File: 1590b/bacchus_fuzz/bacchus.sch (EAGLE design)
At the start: 27 parts, among them J1 DC_MONO, Q1 NPN, Q2 NPN

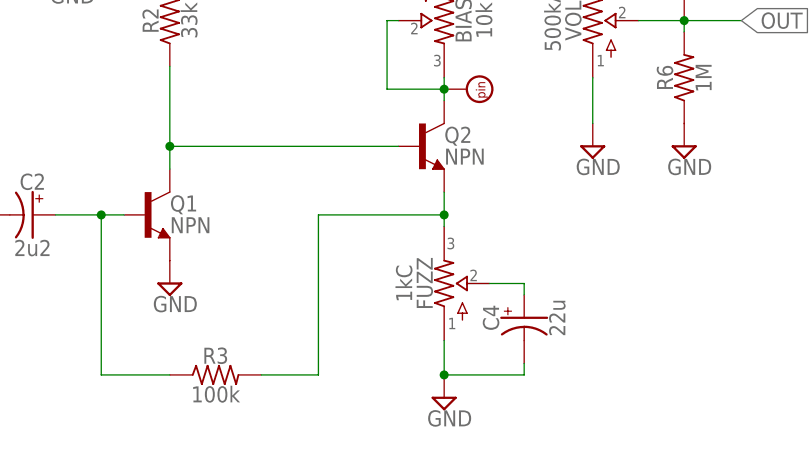
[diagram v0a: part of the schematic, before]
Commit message: added SQUONK (envelope filter)
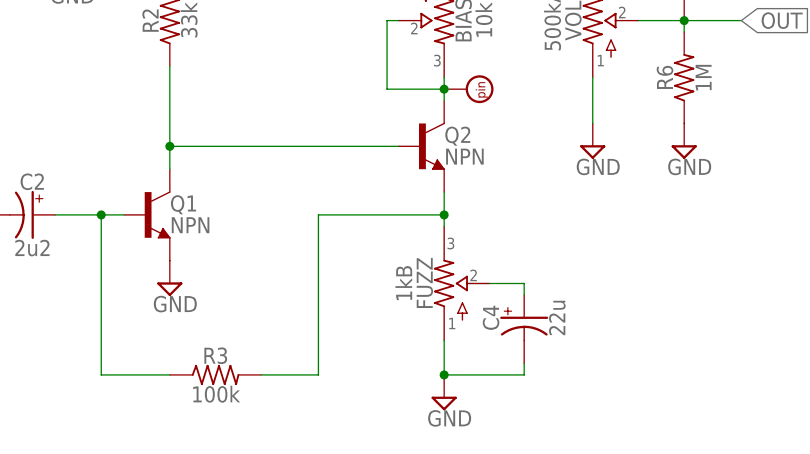
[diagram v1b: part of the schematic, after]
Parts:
- FUZZ: value 1kC -> 1kB
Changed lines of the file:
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@@
 <setting verticaltext="up"/>
 </settings>
-<grid distance="0.05" unitdist="inch" unit="inch" style="lines" multiple="1" display="no" altdistance="0.01" altunitdist="inch" altunit="inch"/>
+<grid distance="0.1" unitdist="inch" unit="inch" style="lines" multiple="1" display="no" altdistance="0.01" altunitdist="inch" altunit="inch"/>
 <layers>
 <layer number="1" name="Top" color="4" fill="1" visible="no" active="no"/>
@@
 <part name="R5" library="resistors" deviceset="R_" device=".3B" value="1k"/>
 <part name="R3" library="resistors" deviceset="R_" device=".3B" value="100k"/>
-<part name="FUZZ" library="potentiometers" deviceset="POTS" device="9MM_MOUNTED" value="1kC"/>
+<part name="FUZZ" library="potentiometers" deviceset="POTS" device="9MM_MOUNTED" value="1kB"/>
 <part name="VOL" library="potentiometers" deviceset="POTS" device="9MM_MOUNTED" value="500kA"/>
 <part name="CONT" library="potentiometers" deviceset="POTS" device="9MM_MOUNTED" value="1kB"/>
